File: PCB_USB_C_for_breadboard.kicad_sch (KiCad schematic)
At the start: 13 parts, among them J1 USB_C_Receptacle_USB2.0_16P, J2 Conn_01x02_Pin, J3 Conn_01x02_Pin, J4 Conn_01x03_Pin, J5 Conn_01x05_Socket, SW1 SW_SPDT, U1 NJM2845DL1-33

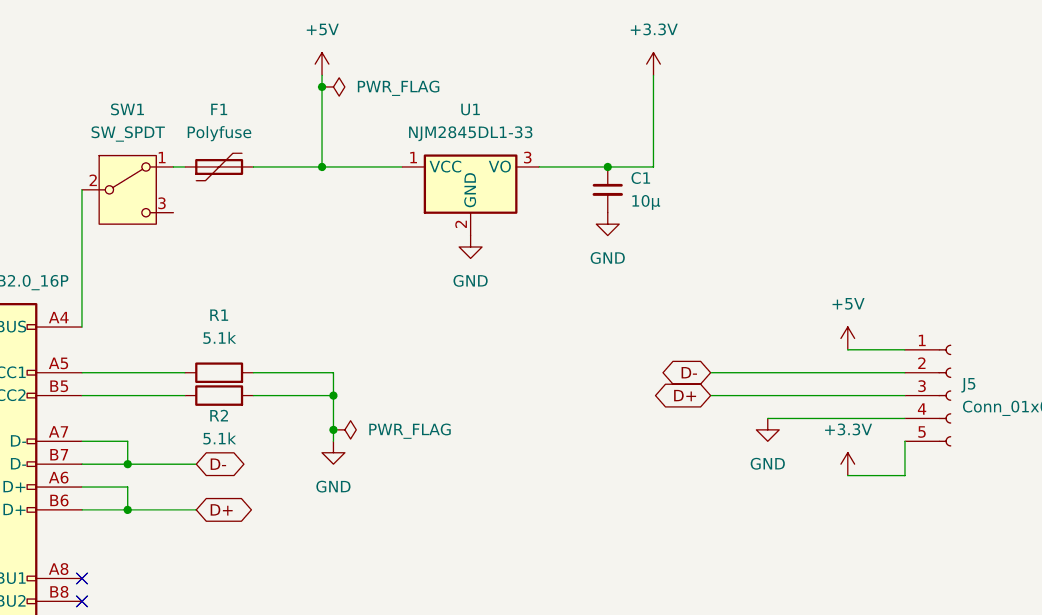
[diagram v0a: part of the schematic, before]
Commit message: Rev. 2
* 基板サイズを拡大
* SW1の位置を調整
* SMDのポリヒューズを取り付け可能に
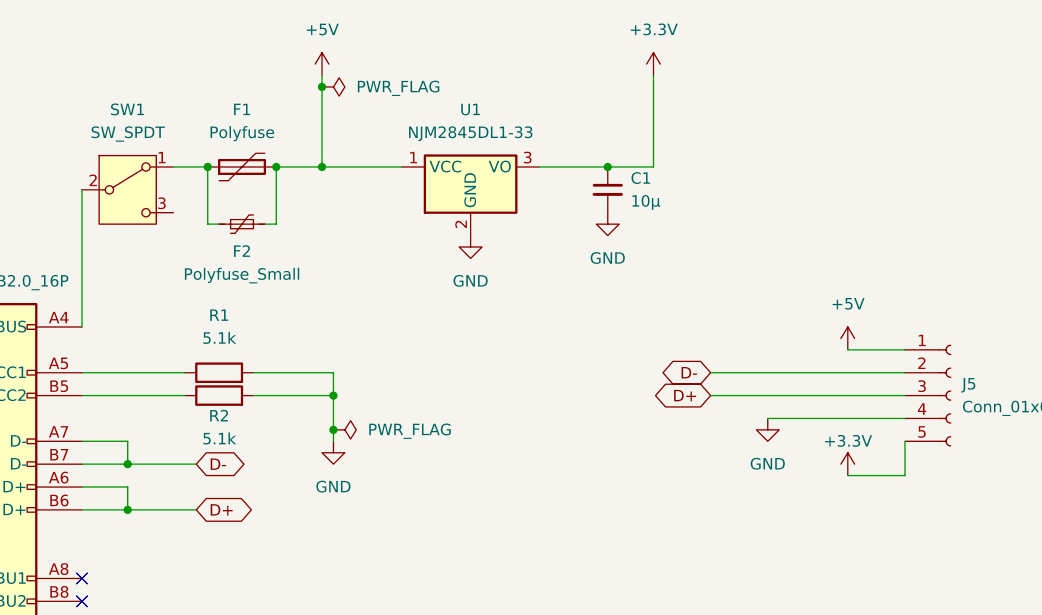
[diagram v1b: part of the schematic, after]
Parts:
- added F2: Polyfuse_Small, Fuse:Fuse_1206_3216Metric_Pad1.42x1.75mm_HandSolder, symbol Device:Polyfuse_Small
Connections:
- net +5V: now also F2.2
- net at F1.1, SW1.1 (A): now also F2.1
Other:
- moved on the sheet: F1
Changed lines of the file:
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@@
 	(title_block
 		(title "USB Type-C Power Adaptor for Breadboard")
-		(date "2025-06-29")
-		(rev "1")
+		(date "2025-07-10")
+		(rev "2")
 		(company "K.Takata")
 	)
@@
 	)
 	(junction
+		(at 91.44 53.34)
+		(diameter 0)
+		(color 0 0 0 0)
+	)
+	(junction
 		(at 74.93 91.44)
 		(diameter 0)
@@
 		(color 0 0 0 0)
 	)
+	(junction
+		(at 83.82 53.34)
+		(diameter 0)
+		(color 0 0 0 0)
+	)
 	(no_connect
 		(at 69.85 99.06)
@@
 	(wire
 		(pts
+			(xy 85.09 59.69) (xy 83.82 59.69)
+		)
+		(stroke
+			(width 0)
+			(type default)
+		)
+	)
+	(wire
+		(pts
 			(xy 133.35 135.89) (xy 146.05 135.89)
 		)
@@
 	(wire
 		(pts
+			(xy 91.44 59.69) (xy 91.44 53.34)
+		)
+		(stroke
+			(width 0)
+			(type default)
+		)
+	)
+	(wire
+		(pts
 			(xy 161.29 135.89) (xy 173.99 135.89)
 		)
@@
 	(wire
 		(pts
-			(xy 80.01 53.34) (xy 81.28 53.34)
+			(xy 80.01 53.34) (xy 83.82 53.34)
 		)
 		(stroke
@@
 	(wire
 		(pts
+			(xy 83.82 59.69) (xy 83.82 53.34)
+		)
+		(stroke
+			(width 0)
+			(type default)
+		)
+	)
+	(wire
+		(pts
 			(xy 88.9 76.2) (xy 97.79 76.2)
 		)
@@
 	(wire
 		(pts
-			(xy 88.9 53.34) (xy 96.52 53.34)
+			(xy 91.44 53.34) (xy 96.52 53.34)
 		)
 		(stroke
@@
 		(pts
 			(xy 69.85 55.88) (xy 69.85 71.12)
+		)
+		(stroke
+			(width 0)
+			(type default)
+		)
+	)
+	(wire
+		(pts
+			(xy 90.17 59.69) (xy 91.44 59.69)
 		)
 		(stroke
@@
 	(symbol
 		(lib_id "Device:Polyfuse")
-		(at 85.09 53.34 90)
+		(at 87.63 53.34 90)
 		(unit 1)
 		(exclude_from_sim no)
@@
 		(fields_autoplaced yes)
 		(property "Reference" "F1"
-			(at 85.09 46.99 90)
+			(at 87.63 46.99 90)
 			(effects
 				(font
@@
 		)
 		(property "Value" "Polyfuse"
-			(at 85.09 49.53 90)
+			(at 87.63 49.53 90)
 			(effects
 				(font
@@
 		)
 		(property "Footprint" "Capacitor_THT:C_Disc_D4.3mm_W1.9mm_P5.00mm"
-			(at 90.17 52.07 0)
+			(at 92.71 52.07 0)
 			(effects
 				(font
@@
 		)
 		(property "Datasheet" "~"
-			(at 85.09 53.34 0)
+			(at 87.63 53.34 0)
 			(effects
 				(font
@@
 		)
 		(property "Description" "Resettable fuse, polymeric positive temperature coefficient"
-			(at 85.09 53.34 0)
+			(at 87.63 53.34 0)
 			(effects
 				(font
@@
 	)
 	(symbol
+		(lib_id "Device:Polyfuse_Small")
+		(at 87.63 59.69 90)
+		(unit 1)
+		(exclude_from_sim no)
+		(in_bom yes)
+		(on_board yes)
+		(dnp no)
+		(property "Reference" "F2"
+			(at 87.63 62.738 90)
+			(effects
+				(font
+					(size 1.27 1.27)
+				)
+			)
+		)
+		(property "Value" "Polyfuse_Small"
+			(at 87.63 65.278 90)
+			(effects
+				(font
+					(size 1.27 1.27)
+				)
+			)
+		)
+		(property "Footprint" "Fuse:Fuse_1206_3216Metric_Pad1.42x1.75mm_HandSolder"
+			(at 92.71 58.42 0)
+			(effects
+				(font
+					(size 1.27 1.27)
+				)
+				(justify left)
+				(hide yes)
+			)
+		)
+		(property "Datasheet" "~"
+			(at 87.63 59.69 0)
+			(effects
+				(font
+					(size 1.27 1.27)
+				)
+				(hide yes)
+			)
+		)
+		(property "Description" "Resettable fuse, polymeric positive temperature coefficient, small symbol"
+			(at 87.63 59.69 0)
+			(effects
+				(font
+					(size 1.27 1.27)
+				)
+				(hide yes)
+			)
+		)
+		(pin "1"
+		)
+		(pin "2"
+		)
+		(instances
+			(project ""
+				(path "/aa257192-91f6-4d4e-966a-2f3380a6a121"
+					(reference "F2")
+					(unit 1)
+				)
+			)
+		)
+	)
+	(symbol
 		(lib_id "Connector:USB_C_Receptacle_USB2.0_16P")
 		(at 54.61 86.36 0)
@@
 		(on_board yes)
 		(dnp no)
-		(fields_autoplaced yes)
 		(property "Reference" "#PWR013"
 			(at 154.94 91.44 0)
@@
 		)
 		(property "Value" "+3.3V"
-			(at 154.94 82.55 0)
-			(effects
-				(font
+			(at 154.94 83.82 0)
+			(effects
+				(font

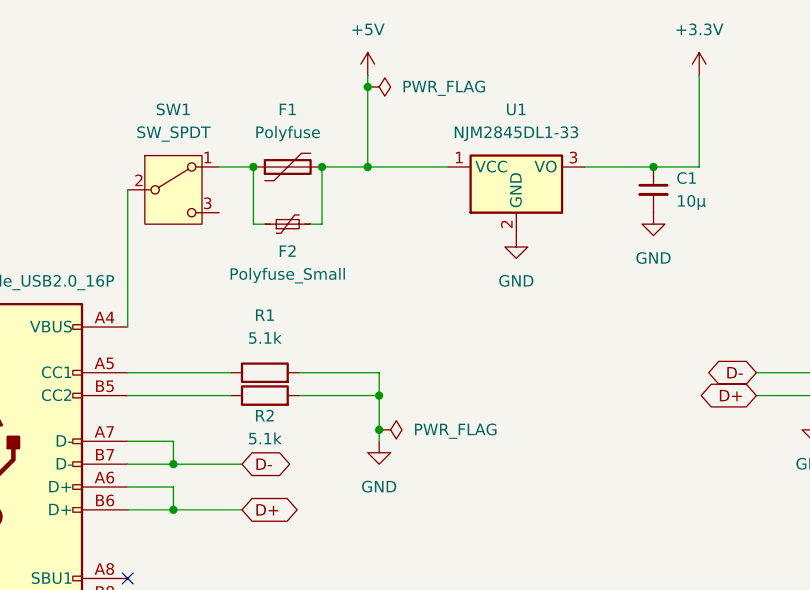
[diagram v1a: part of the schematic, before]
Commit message: Rev. 3
* U1をNJM2845DL1-33からLM1117GS-3.3に変更
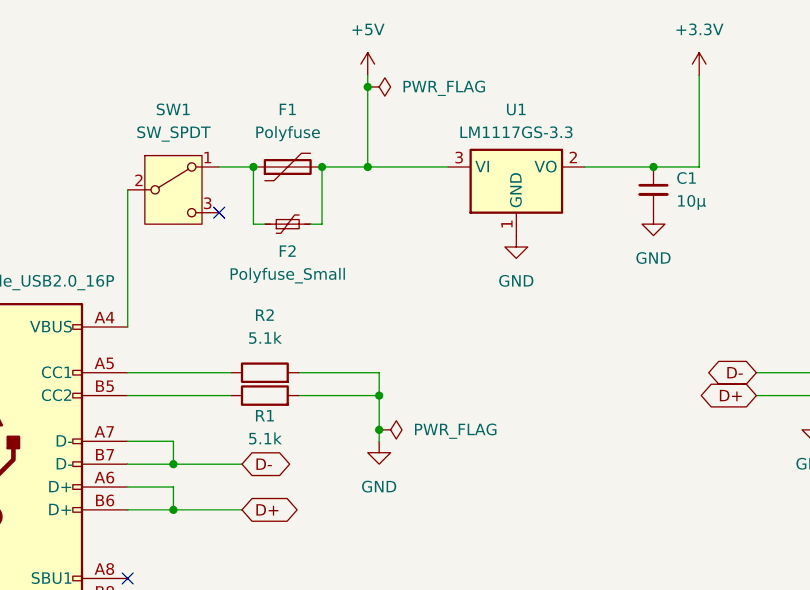
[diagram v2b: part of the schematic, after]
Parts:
- removed U1: NJM2845DL1-33, Package_TO_SOT_SMD:TO-252-2, symbol Regulator_Linear:BD33FC0FP
- added U1: LM1117GS-3.3, Package_TO_SOT_SMD:SOT-223-3_TabPin2, symbol Regulator_Linear:AP1117-33
- renumbered R2 to R1, R1 to R2
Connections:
- net +3.3V: now also U1.2 (VO)
- net +5V: now also U1.3 (VI)
- net GND: now also U1.1 (GND)
- no-connect marks 2 -> 3

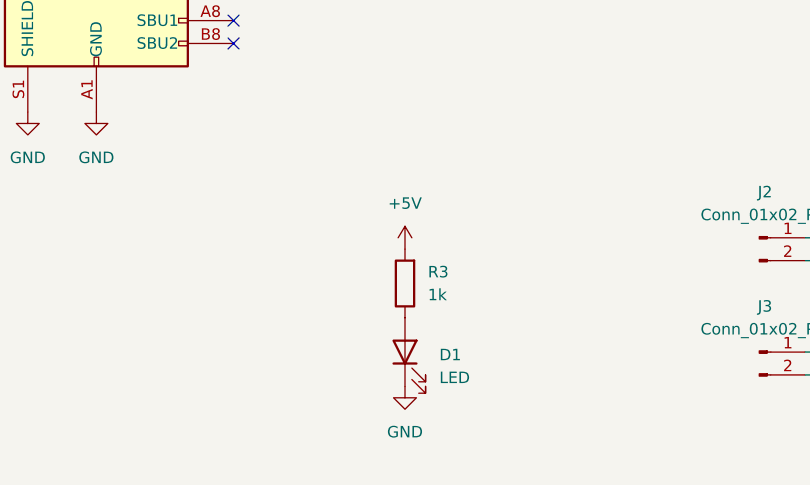
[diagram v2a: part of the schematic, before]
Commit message: 微調整
R3を上下反転。
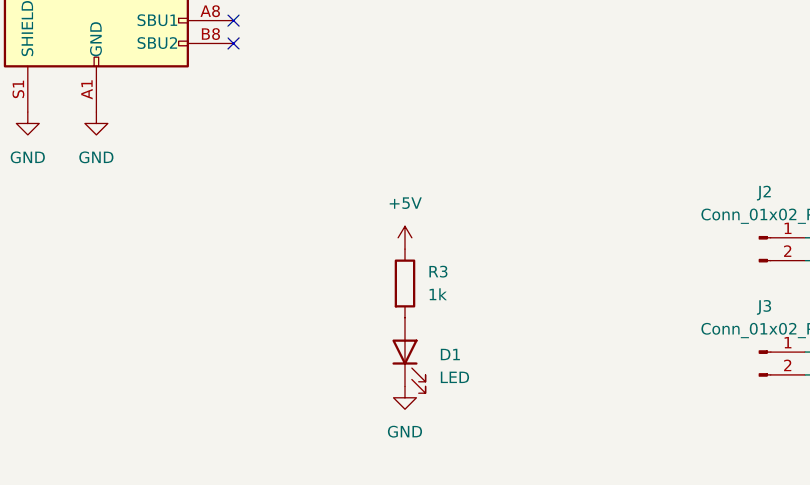
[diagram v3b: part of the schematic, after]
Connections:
- net +5V: now also R3.1; no longer R3.2
- net at D1.2 (A): now also R3.2; no longer R3.1
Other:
- moved on the sheet: R3
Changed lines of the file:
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@@
 	(title_block
 		(title "USB Type-C Power Adaptor for Breadboard")
-		(date "2025-07-14")
+		(date "2025-08-02")
 		(rev "3")
 		(company "K.Takata")
@@
 	(symbol
 		(lib_id "Device:R")
-		(at 88.9 128.27 180)
+		(at 88.9 128.27 0)
 		(unit 1)
 		(exclude_from_sim no)
@@
 					(size 1.27 1.27)
 				)
-				(justify right)
+				(justify left)
 			)
 		)
@@
 					(size 1.27 1.27)
 				)
-				(justify right)
+				(justify left)
 			)
 		)
 		(property "Footprint" "Resistor_THT:R_Axial_DIN0204_L3.6mm_D1.6mm_P2.54mm_Vertical"
-			(at 90.678 128.27 90)
-			(effects
-				(font
+			(at 87.122 128.27 90)
+			(effects
+				(font
